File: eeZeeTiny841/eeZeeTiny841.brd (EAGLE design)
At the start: 28.7 x 16.3 mm, 12 parts, among them IC1 ATtiny841, J2 avrisp, Q1 16MHz

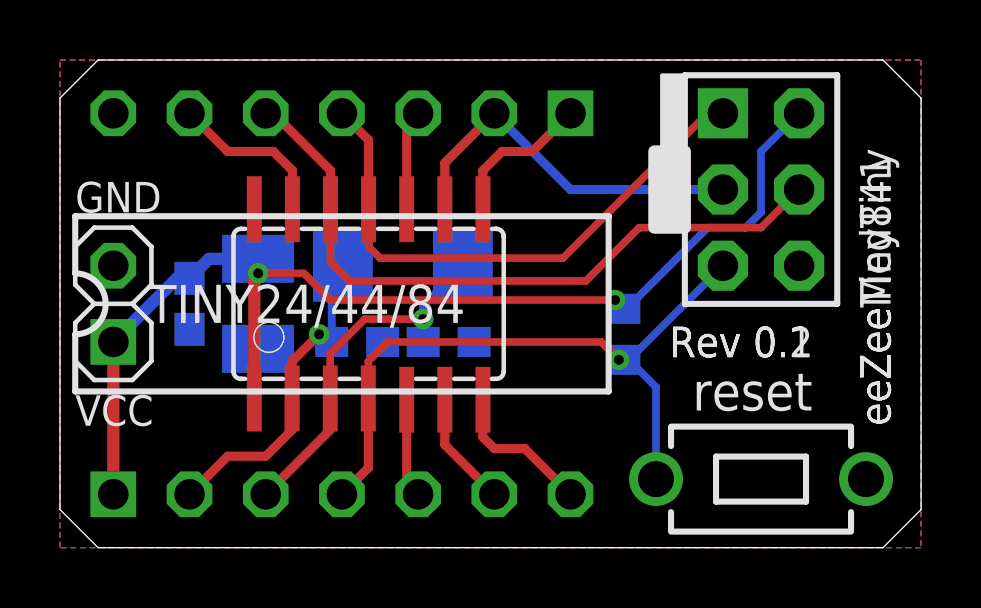
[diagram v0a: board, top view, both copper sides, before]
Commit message: Minor mods to board/schematic. avrdude config from AVRfreaks forum.
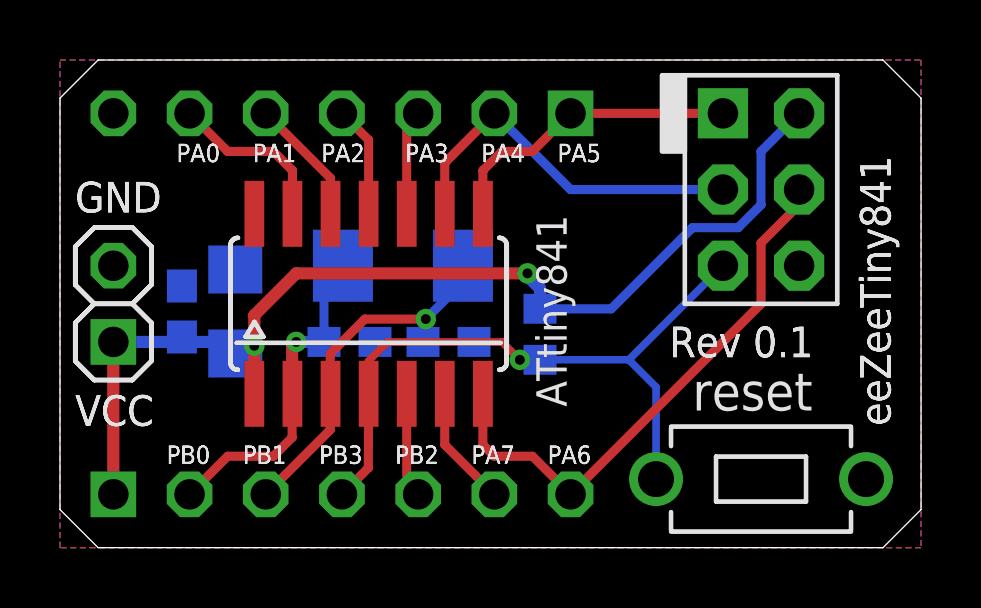
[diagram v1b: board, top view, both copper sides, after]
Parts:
- C2: device mes_rcl:SMC_B -> rcl:C1206
- IC1: device bt_avr:SOIC14 -> bt_avr:14SOICN
- moved R1 2.79 mm to (16.0, 7.11)
- moved IC1 1.91 mm to (10.3, 8.13)
- moved C2 0.80 mm to (5.84, 7.87), turned to 90 degrees
- moved C1 0.36 mm to (4.06, 7.87), turned to 90 degrees
- moved C5 0.25 mm to (9.65, 6.86)
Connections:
- net SCK renamed PA4
- removed net MISO: IC1.11, J2.1, JP5.4
- removed net MOSI: IC1.12, J2.4, JP5.5
- new net PA5: IC1.8, J2.1, JP5.1
- new net PA6: IC1.7, J2.4, JP4.7
- net GND: now also C2.2; no longer C2.-
- net PA0: now also IC1.13, JP5.6; no longer IC1.6, JP4.6
- net PA1: now also IC1.12, JP5.5; no longer IC1.7, JP4.7
- net PA2: now also IC1.11, JP5.4; no longer IC1.8, JP5.1
- net PA7: now also IC1.6, JP4.6; no longer IC1.13, JP5.6
- net VCC: now also C2.1; no longer C2.+
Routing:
- net MOSI: track 23.1 -> 0.00 mm
- net MISO: track 18.8 -> 0.00 mm
- net PA6: track 0.00 -> 18.6 mm
- net PA5: track 0.00 -> 10.2 mm
- net VCC: track 38.2 -> 36.3 mm
- net PA0: track 3.84 -> 5.66 mm
- net PA7: track 5.51 -> 4.03 mm
- net PA2: track 5.00 -> 3.72 mm
- net XTAL2: track 11.5 -> 12.3 mm
- net PA1: track 4.96 -> 4.24 mm
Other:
- board text added: "ATtiny841"
- board text added: "PA0"
- board text added: "PA1"
- board text added: "PA2"
- board text added: "PA3"
- board text added: "PA4"
- board text added: "PA5"
- board text added: "PA6"
- board text added: "PA7"
- board text added: "PB0"
- board text added: "PB1"
- board text added: "PB2"
- board text added: "PB3"
- board text removed: "Rev 0.2"
- board text removed: "TINY24/44/84"
- board text removed: "eeZeeMedTiny"
